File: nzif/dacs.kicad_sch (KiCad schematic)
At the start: 62 parts, among them Q601 FZT951TA, U601 ADAU1962AWBSTZ-RL, U602 ADA4807-1

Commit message: top sheet wiring
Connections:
- net DBCLK renamed DAC_BCLK
- net DLRCLK renamed DAC_LRCLK
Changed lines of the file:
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@@
-		)
-	)
-	(hierarchical_label "DLRCLK"
-		(shape input)
-		(at 133.35 106.68 180)
-		(effects
-			(font
-				(size 1.27 1.27)
-			)
-			(justify right)
 		)
 	)
@@
 		(shape input)
 		(at 139.7 58.42 180)
-		(effects
-			(font
-				(size 1.27 1.27)
-			)
-			(justify right)
-		)
-	)
-	(hierarchical_label "DBCLK"
-		(shape input)
-		(at 133.35 104.14 180)
 		(effects
 			(font
@@
 		)
 	)
+	(hierarchical_label "DAC_BCLK"
+		(shape input)
+		(at 133.35 104.14 180)
+		(effects
+			(font
+				(size 1.27 1.27)
+			)
+			(justify right)
+		)
+	)
 	(hierarchical_label "DAC_P315-"
 		(shape output)
@@
 		)
 	)
+	(hierarchical_label "DAC_LRCLK"
+		(shape input)
+		(at 133.35 106.68 180)
+		(effects
+			(font
+				(size 1.27 1.27)
+			)
+			(justify right)
+		)
+	)

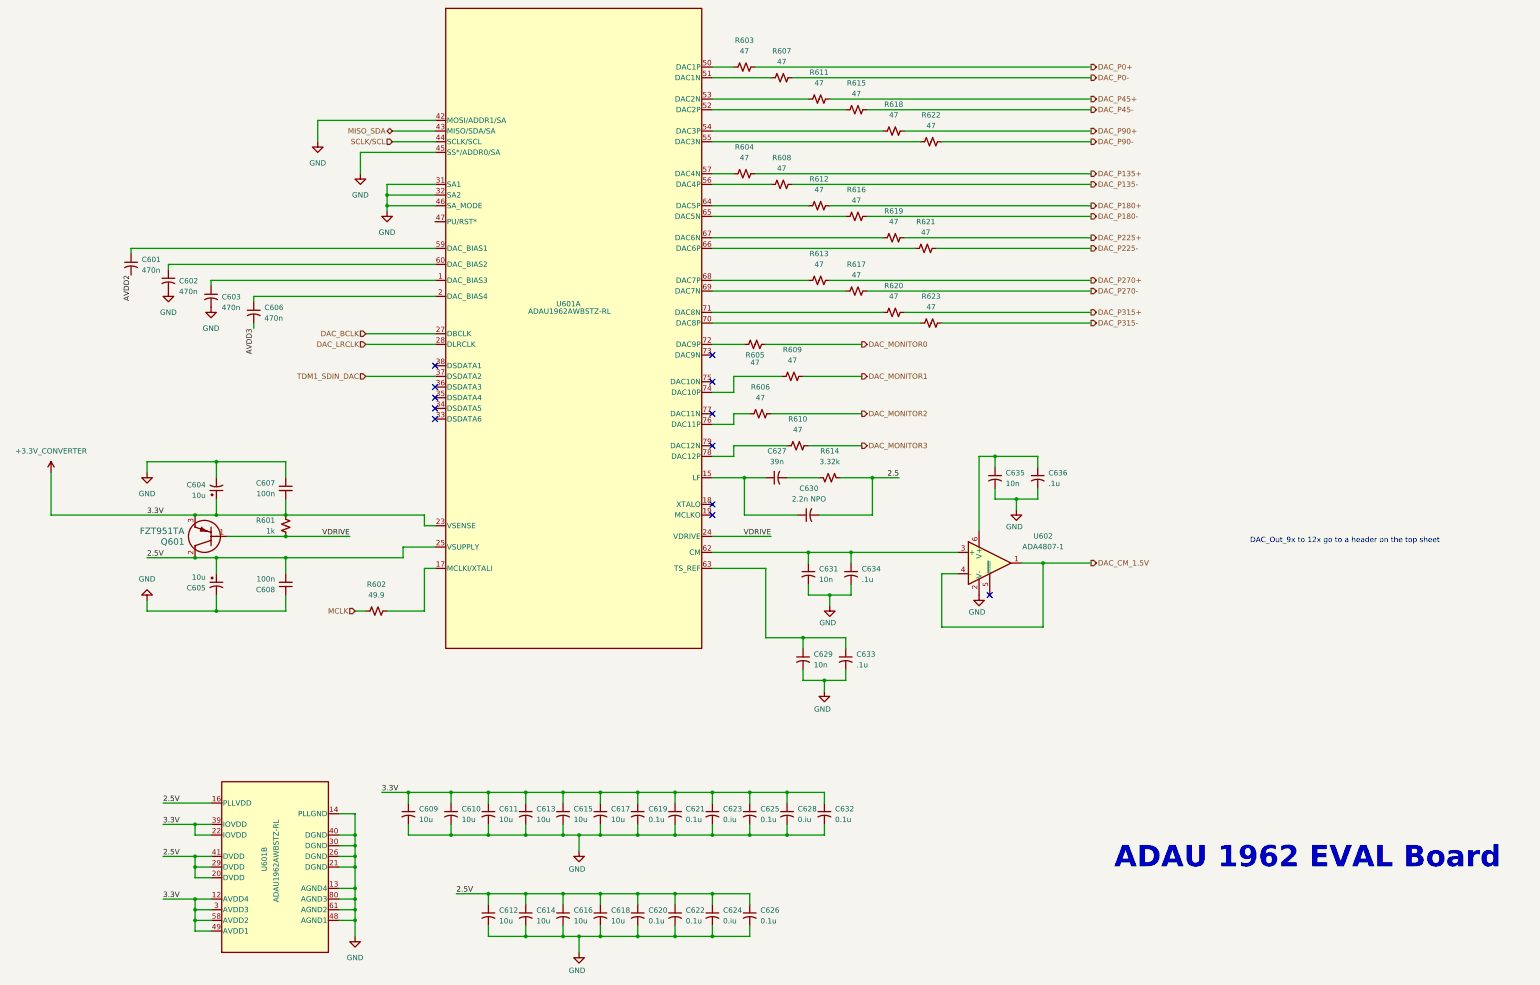
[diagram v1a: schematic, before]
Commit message: Fix ERC errors: symbol pin types and schematic corrections
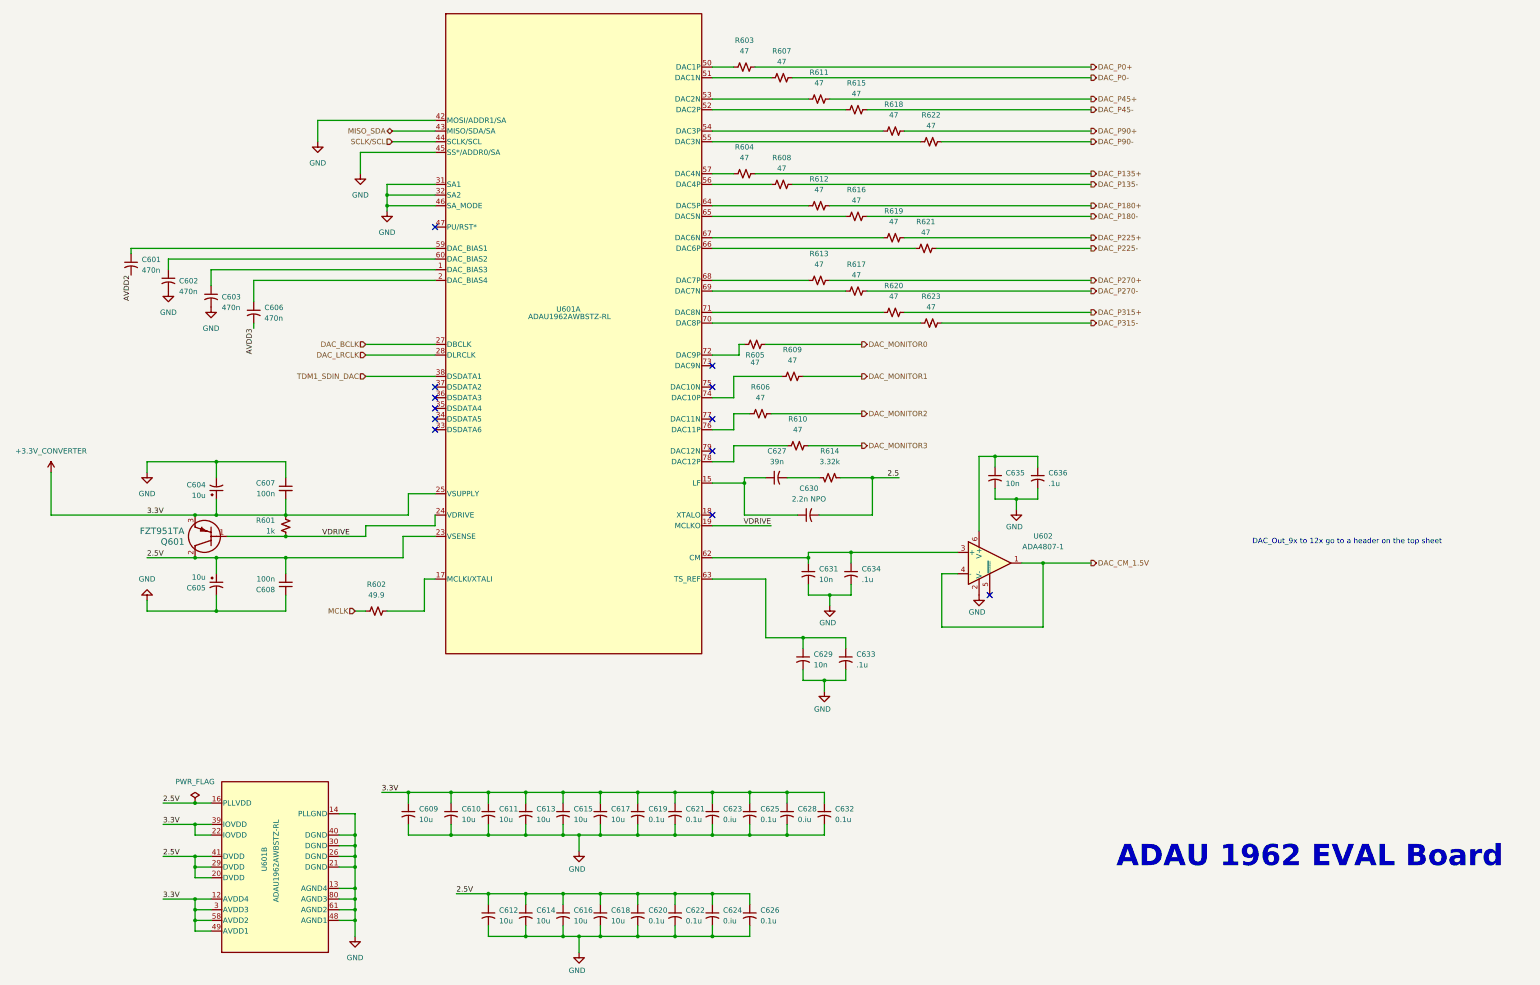
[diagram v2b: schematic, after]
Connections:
- net +3.3V_CONVERTER: now also U601.25 (VSUPPLY); no longer U601.23 (VSENSE)
- net 2.5V: now also U601.23 (VSENSE); no longer U601.25 (VSUPPLY)
- net TDM1_SDIN_DAC: now also U601.38 (DSDATA1); no longer U601.37 (DSDATA2)
- net VDRIVE: now also U601.19 (MCLKO)
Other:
- moved on the sheet: U601A

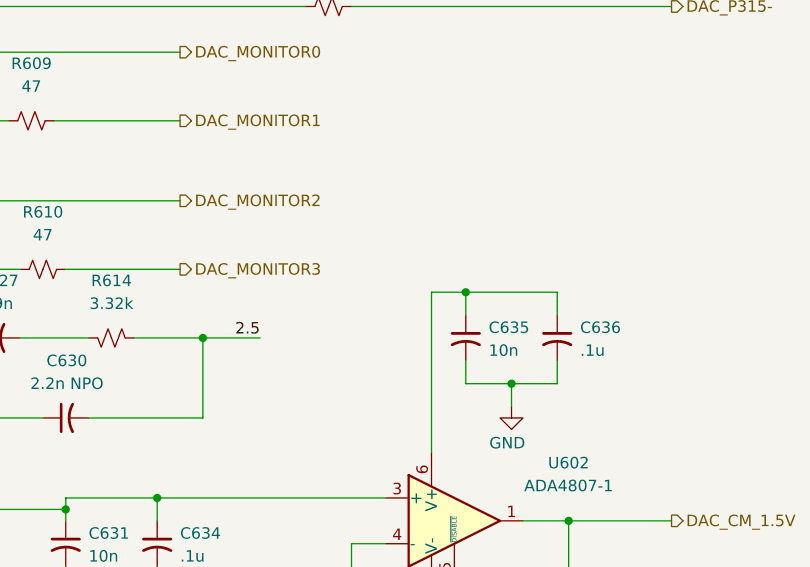
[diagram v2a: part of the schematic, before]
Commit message: fixed minor erc related issues
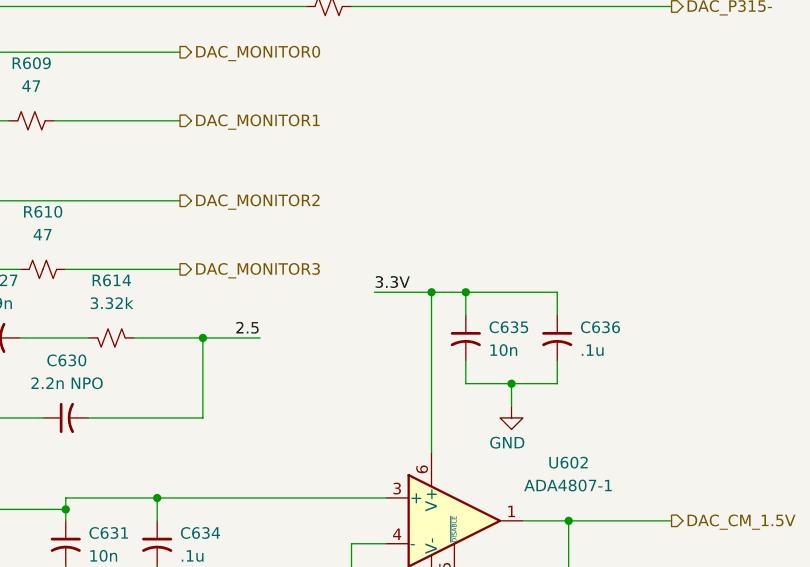
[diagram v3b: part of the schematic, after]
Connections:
- net +3.3V_CONVERTER: now also C635.1, C636.1, U602.6 (V+)
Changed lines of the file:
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@@
+	)
+	(junction
+		(at 279.4 133.35)
+		(diameter 0)
+		(color 0 0 0 0)
 	)
 	(junction
@@
 	(wire
 		(pts
+			(xy 279.4 133.35) (xy 283.21 133.35)
+		)
+		(stroke
+			(width 0)
+			(type default)
+		)
+	)
+	(wire
+		(pts
 			(xy 130.81 241.3) (xy 130.81 243.84)
 		)
@@
 	(wire
 		(pts
+			(xy 273.05 133.35) (xy 279.4 133.35)
+		)
+		(stroke
+			(width 0)
+			(type default)
+		)
+	)
+	(wire
+		(pts
 			(xy 137.16 213.36) (xy 143.51 213.36)
 		)
@@
 		(pts
 			(xy 130.81 170.18) (xy 133.35 170.18)
-		)
-		(stroke
-			(width 0)
-			(type default)
-		)
-	)
-	(wire
-		(pts
-			(xy 279.4 133.35) (xy 283.21 133.35)
 		)
 		(stroke
@@
 		(effects
 			(font
+				(size 1.27 1.27)
+			)
+			(justify left bottom)
+		)
+	)
+	(label "3.3V"
+		(at 273.05 133.35 0)
+		(effects
+			(font

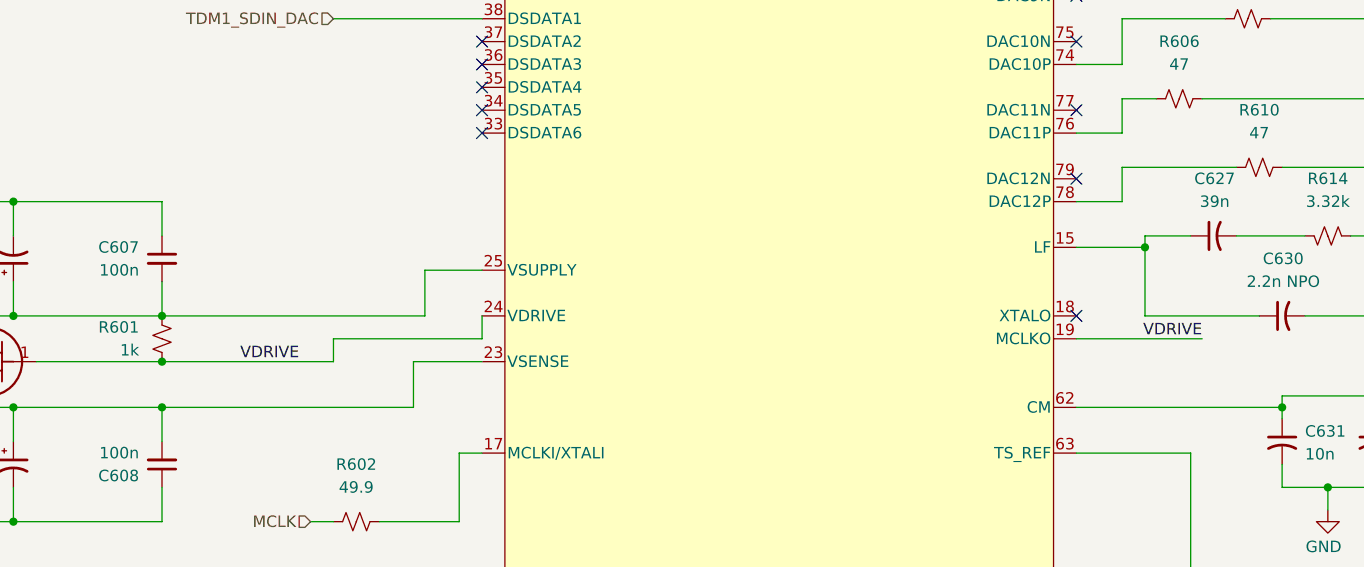
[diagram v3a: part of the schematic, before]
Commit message: fixed remaining ERC errors
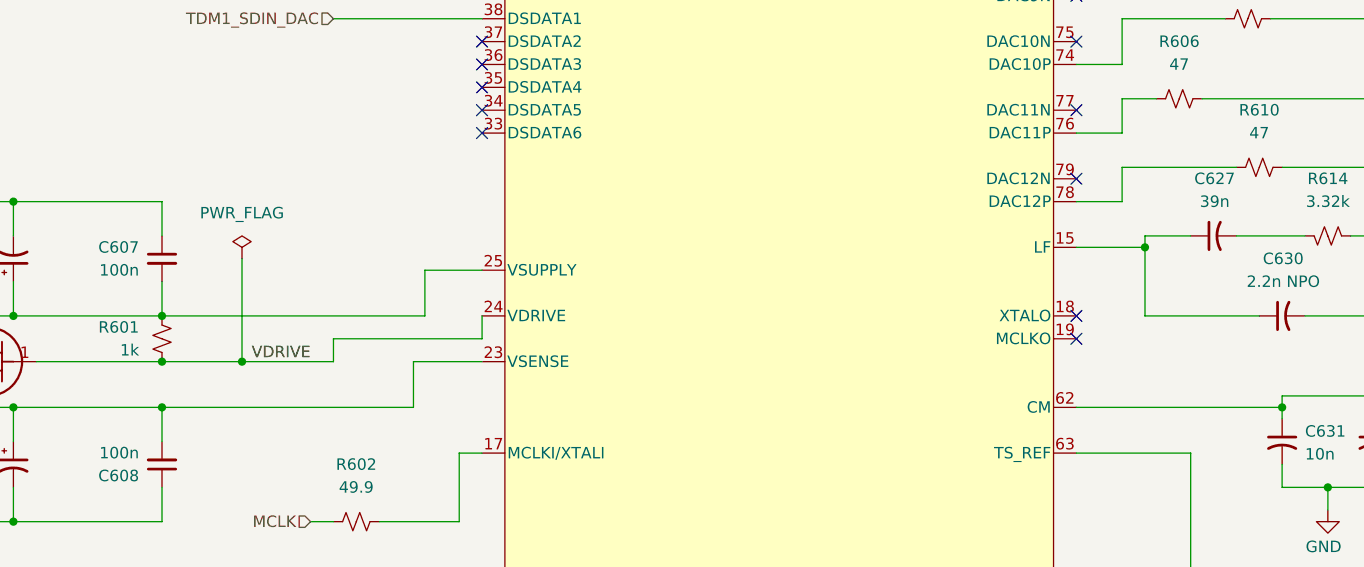
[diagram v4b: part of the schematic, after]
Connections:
- net VDRIVE: no longer U601.19 (MCLKO)
- no-connect marks 12 -> 13
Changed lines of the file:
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@@
 	)
 	(junction
+		(at 123.19 152.4)
+		(diameter 0)
+		(color 0 0 0 0)
+	)
+	(junction
 		(at 143.51 213.36)
 		(diameter 0)
@@
 	)
 	(no_connect
+		(at 215.9 149.86)
+	)
+	(no_connect
 		(at 149.86 116.84)
 	)
@@
 	(wire
 		(pts
+			(xy 123.19 152.4) (xy 133.35 152.4)
+		)
+		(stroke
+			(width 0)
+			(type default)
+		)
+	)
+	(wire
+		(pts
 			(xy 215.9 101.6) (xy 265.43 101.6)
 		)
@@
 	(wire
 		(pts
-			(xy 114.3 152.4) (xy 133.35 152.4)
+			(xy 114.3 152.4) (xy 123.19 152.4)
 		)
 		(stroke
@@
 	(wire
 		(pts
-			(xy 215.9 149.86) (xy 229.87 149.86)
-		)
-		(stroke
-			(width 0)
-			(type default)
-		)
-	)
-	(wire
-		(pts
 			(xy 143.51 213.36) (xy 153.67 213.36)
 		)
@@
 	(wire
 		(pts
+			(xy 123.19 140.97) (xy 123.19 152.4)
+		)
+		(stroke
+			(width 0)
+			(type default)
+		)
+	)
+	(wire
+		(pts
 			(xy 130.81 170.18) (xy 133.35 170.18)
 		)
@@
 		)
 	)
-	(label "VDRIVE"
-		(at 229.87 149.86 180)
-		(effects
-			(font
-				(size 1.27 1.27)
-			)
-			(justify right bottom)
-		)
-	)
 	(label "2.5V"
 		(at 85.09 228.6 0)
@@
 	)
 	(label "VDRIVE"
-		(at 129.54 152.4 180)
+		(at 130.81 152.4 180)
 		(effects
 			(font
@@
 					(unit 1)
 				)
+			)
+		)
+	)
+	(symbol
+		(lib_id "power:PWR_FLAG")
+		(at 123.19 140.97 0)
+		(unit 1)
+		(body_style 1)
+		(exclude_from_sim no)
+		(in_bom yes)
+		(on_board yes)
+		(in_pos_files yes)
+		(dnp no)
+		(fields_autoplaced yes)
+		(property "Reference" "#FLG01207"
+			(at 123.19 139.065 0)
+			(hide yes)
+			(show_name no)
+			(do_not_autoplace no)
+			(effects
+				(font
+					(size 1.27 1.27)
+				)
+			)
+		)
+		(property "Value" "PWR_FLAG"
+			(at 123.19 135.89 0)
+			(show_name no)
+			(do_not_autoplace no)
+			(effects
+				(font
+					(size 1.27 1.27)
+				)
+			)
+		)
+		(property "Footprint" ""
+			(at 123.19 140.97 0)
+			(hide yes)
+			(show_name no)
+			(do_not_autoplace no)
+			(effects
+				(font
+					(size 1.27 1.27)
+				)
+			)
+		)
+		(property "Datasheet" ""
+			(at 123.19 140.97 0)
+			(hide yes)
+			(show_name no)
+			(do_not_autoplace no)
+			(effects
+				(font
+					(size 1.27 1.27)
+				)
+			)
+		)
+		(property "Description" "Special symbol for telling ERC where power comes from"
+			(at 123.19 140.97 0)
+			(hide yes)
+			(show_name no)
+			(do_not_autoplace no)
+			(effects
+				(font
+					(size 1.27 1.27)
+				)
+			)
+		)
+		(pin "1"
+		)
+		(instances
+			(project "nzif"
+				(path "/fe42ca2f-2bb8-4d5a-9e84-807788ed632f/1097e363-2947-4914-97f0-a09e0bb38c3a"
+					(reference "#FLG01207")
+					(unit 1)
+				)

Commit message: erc improvements
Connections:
- net AVDD2 is gone; now on net +3.3V_CONVERTER: C601.2
- net AVDD3 is gone; now on net +3.3V_CONVERTER: C606.2
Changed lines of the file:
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@@
-	(wire
-		(pts
-			(xy 106.68 101.6) (xy 106.68 102.87)
-		)
-		(stroke
-			(width 0)
-			(type default)
-		)
-	)
 	(wire
 		(pts
@@
 	(wire
 		(pts
+			(xy 77.47 90.17) (xy 77.47 95.25)
+		)
+		(stroke
+			(width 0)
+			(type default)
+		)
+	)
+	(wire
+		(pts
 			(xy 153.67 213.36) (xy 162.56 213.36)
 		)
@@
 		(pts
 			(xy 127 241.3) (xy 130.81 241.3)
+		)
+		(stroke
+			(width 0)
+			(type default)
+		)
+	)
+	(wire
+		(pts
+			(xy 106.68 101.6) (xy 106.68 106.68)
 		)
 		(stroke
@@
 		)
 	)
-	(label "AVDD2"
-		(at 77.47 90.17 270)
+	(label "3.3V"
+		(at 77.47 95.25 90)
 		(effects
 			(font
 				(size 1.27 1.27)
 			)
-			(justify right bottom)
+			(justify left bottom)
 		)
 	)
@@
 		)
 	)
-	(label "AVDD3"
-		(at 106.68 102.87 270)
+	(label "3.3V"
+		(at 106.68 106.68 90)
 		(effects
 			(font
 				(size 1.27 1.27)
 			)
-			(justify right bottom)
-		)
-	)
+			(justify left bottom)
+		)
+	)

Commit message: fixed error with selfboot circuit
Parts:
- added R624: 0, symbol Device:R_Small_US
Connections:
- net +3.3V_CONVERTER: now also R624.1; no longer C601.2, C604.1, C606.2, C607.2, C609.1, C610.1, C611.1, C613.1, C615.1, C617.1, C619.1, C621.1, C623.1, C625.1, C628.1, C632.1, C635.1, C636.1, Q601.3, R601.1, U601.12 (AVDD4), U601.22 (IOVDD), U601.25 (VSUPPLY), U601.3 (AVDD3), U601.39 (IOVDD), U601.49 (AVDD1), U601.58 (AVDD2), U602.6 (V+)
- new net 3.3V: C601.2, C604.1, C606.2, C607.2, C609.1, C610.1, C611.1, C613.1, C615.1, C617.1, C619.1, C621.1, C623.1, C625.1, C628.1, C632.1, C635.1, C636.1, Q601.3, R601.1, R624.2, U601.12 (AVDD4), U601.22 (IOVDD), U601.25 (VSUPPLY), U601.3 (AVDD3), U601.39 (IOVDD), U601.49 (AVDD1), U601.58 (AVDD2), U602.6 (V+)
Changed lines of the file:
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@@
 	)
 	(junction
+		(at 72.39 147.32)
+		(diameter 0)
+		(color 0 0 0 0)
+	)
+	(junction
 		(at 198.12 247.65)
 		(diameter 0)
@@
 	(wire
 		(pts
+			(xy 72.39 147.32) (xy 92.71 147.32)
+		)
+		(stroke
+			(width 0)
+			(type default)
+		)
+	)
+	(wire
+		(pts
 			(xy 215.9 68.58) (xy 229.87 68.58)
 		)
@@
 	(wire
 		(pts
-			(xy 58.42 147.32) (xy 92.71 147.32)
+			(xy 58.42 147.32) (xy 62.23 147.32)
 		)
 		(stroke
@@
 	(wire
 		(pts
+			(xy 67.31 147.32) (xy 72.39 147.32)
+		)
+		(stroke
+			(width 0)
+			(type default)
+		)
+	)
+	(wire
+		(pts
 			(xy 243.84 48.26) (xy 306.07 48.26)
 		)
@@
 	)
 	(symbol
+		(lib_id "power:PWR_FLAG")
+		(at 72.39 147.32 0)
+		(unit 1)
+		(body_style 1)
+		(exclude_from_sim no)
+		(in_bom yes)
+		(on_board yes)
+		(in_pos_files yes)
+		(dnp no)
+		(fields_autoplaced yes)
+		(property "Reference" "#FLG01212"
+			(at 72.39 145.415 0)
+			(hide yes)
+			(show_name no)
+			(do_not_autoplace no)
+			(effects
+				(font
+					(size 1.27 1.27)
+				)
+			)
+		)
+		(property "Value" "PWR_FLAG"
+			(at 72.39 142.24 0)
+			(show_name no)
+			(do_not_autoplace no)
+			(effects
+				(font
+					(size 1.27 1.27)
+				)
+			)
+		)
+		(property "Footprint" ""
+			(at 72.39 147.32 0)
+			(hide yes)
+			(show_name no)
+			(do_not_autoplace no)
+			(effects
+				(font
+					(size 1.27 1.27)
+				)
+			)
+		)
+		(property "Datasheet" ""
+			(at 72.39 147.32 0)
+			(hide yes)
+			(show_name no)
+			(do_not_autoplace no)
+			(effects
+				(font
+					(size 1.27 1.27)
+				)
+			)
+		)
+		(property "Description" "Special symbol for telling ERC where power comes from"
+			(at 72.39 147.32 0)
+			(hide yes)
+			(show_name no)
+			(do_not_autoplace no)
+			(effects
+				(font
+					(size 1.27 1.27)
+				)
+			)
+		)
+		(pin "1"
+		)
+		(instances
+			(project "nzif"
+				(path "/fe42ca2f-2bb8-4d5a-9e84-807788ed632f/1097e363-2947-4914-97f0-a09e0bb38c3a"
+					(reference "#FLG01212")
+					(unit 1)
+				)
+			)
+		)
+	)
+	(symbol
 		(lib_id "Device:C_Small_US")
 		(at 224.79 242.57 0)
@@
 					(unit 1)
 				)
+			)
+		)
+	)
+	(symbol
+		(lib_id "Device:R_Small_US")
+		(at 64.77 147.32 90)
+		(unit 1)
+		(body_style 1)
+		(exclude_from_sim no)
+		(in_bom yes)
+		(on_board yes)
+		(in_pos_files yes)
+		(dnp no)
+		(fields_autoplaced yes)
+		(property "Reference" "R624"
+			(at 64.77 140.97 90)
+			(show_name no)
+			(do_not_autoplace no)
+			(effects
+				(font
+					(size 1.27 1.27)
+				)
+			)
+		)
+		(property "Value" "0"
+			(at 64.77 143.51 90)
+			(show_name no)
+			(do_not_autoplace no)
+			(effects
+				(font
+					(size 1.27 1.27)
+				)
+			)
+		)
+		(property "Footprint" ""
+			(at 64.77 147.32 0)
+			(hide yes)
+			(show_name no)
+			(do_not_autoplace no)
+			(effects
+				(font
+					(size 1.27 1.27)
+				)
+			)
+		)
+		(property "Datasheet" ""
+			(at 64.77 147.32 0)
+			(hide yes)
+			(show_name no)
+			(do_not_autoplace no)
+			(effects
+				(font
+					(size 1.27 1.27)
+				)
+			)
+		)
+		(property "Description" "Resistor, small US symbol"
+			(at 64.77 147.32 0)
+			(hide yes)
+			(show_name no)
+			(do_not_autoplace no)
+			(effects
+				(font
+					(size 1.27 1.27)
+				)
+			)
+		)
+		(property "Digikey Part #" ""
+			(at 64.77 147.32 90)
+			(hide yes)
+			(show_name no)
+			(do_not_autoplace no)
+			(effects
+				(font
+					(size 1.27 1.27)
+				)
+			)
+		)
+		(pin "1"
+		)
+		(pin "2"
+		)
+		(instances
+			(project "nzif"
+				(path "/fe42ca2f-2bb8-4d5a-9e84-807788ed632f/1097e363-2947-4914-97f0-a09e0bb38c3a"
+					(reference "R624")
+					(unit 1)
+				)

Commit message: fixing erc errors
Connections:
- net +3.3V_CONVERTER renamed +3.3V_CONVERTERS
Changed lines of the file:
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@@
 			)
 		)
-		(property "Value" "+3.3V_CONVERTER"
-			(at 58.42 132.08 0)
+		(property "Value" "+3.3V_CONVERTERS"
+			(at 60.96 135.8899 0)
 			(show_name no)
 			(do_not_autoplace no)
@@
 					(size 1.27 1.27)
 				)
+				(justify left)
 			)
 		)
